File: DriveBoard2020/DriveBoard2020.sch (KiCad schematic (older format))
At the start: 56 parts, among them SW0 SW_SPST, SW1 SW_Push, SW2 SW_Push, SW3 SW_Push, SW4 SW_Push, SW5 SW_Push, SW6 SW_Push, U1 MAX232, U2 MAX232, U3 OKI, U4 TM4C129E_Launchpad, U5 MAX232, U6 OKI

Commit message: switch level shifters to 3232's
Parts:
- removed U1, U2, U5: MAX232, Package_SO:SOIC-16_3.9x9.9mm_P1.27mm, symbol Interface_UART:MAX232
- added U? (x3): MAX_3232, symbol MRDT_ICs:MAX_3232
- Conn1: symbol DriveBoard2020-rescue:AndersonPP-MRDT_Connectors -> DriveBoard2020-rescue:AndersonPP-MRDT_Connectors-DriveBoard2020-rescue
- Conn2, Conn3, Conn4, Conn5, Conn6, Conn7: symbol DriveBoard2020-rescue:Molex_SL_05-MRDT_Connectors -> DriveBoard2020-rescue:Molex_SL_05-MRDT_Connectors-DriveBoard2020-rescue
- U3, U6: symbol DriveBoard2020-rescue:OKI-MRDT_Devices -> DriveBoard2020-rescue:OKI-MRDT_Devices-DriveBoard2020-rescue
- U4: symbol DriveBoard2020-rescue:TM4C129E_Launchpad-MRDT_Shields -> DriveBoard2020-rescue:TM4C129E_Launchpad-MRDT_Shields-DriveBoard2020-rescue
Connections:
- wire segments 117 -> 124
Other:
- moved on the sheet: C3, C4, D10, D11, D12, D13, D14, D8, D9, R10, R11, R12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

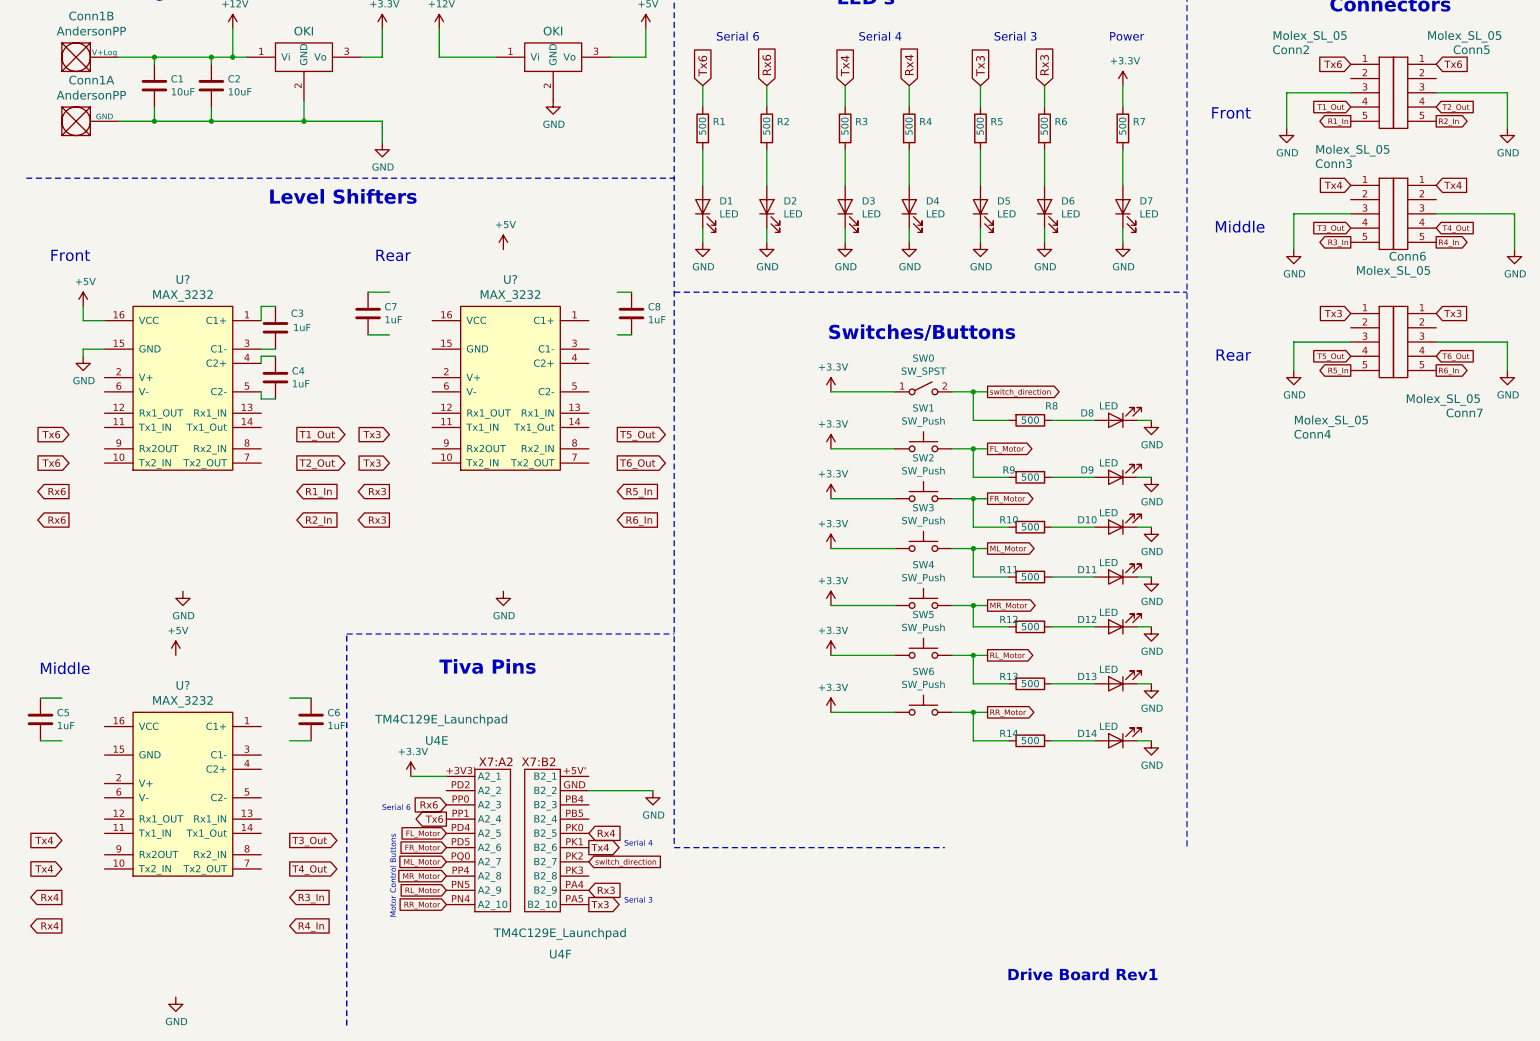
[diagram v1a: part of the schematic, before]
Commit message: changed and wired 3232's
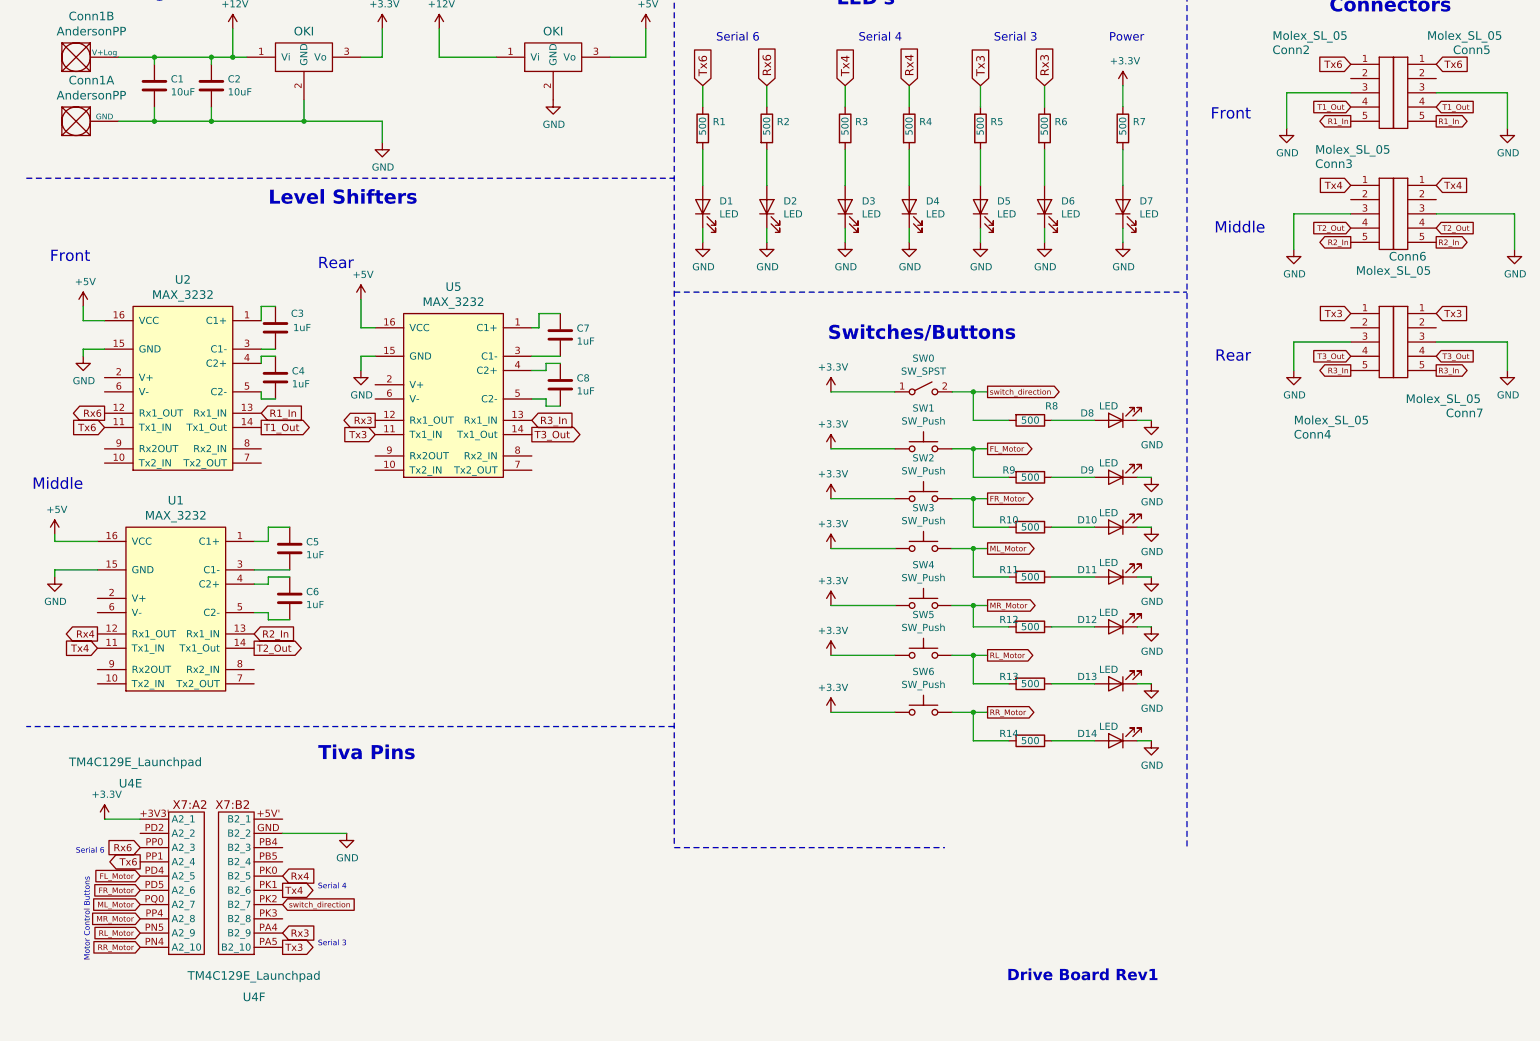
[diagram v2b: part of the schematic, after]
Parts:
- U1, U2, U5: renamed from U?; footprint (none) -> Package_SO:SOIC-16_3.9x9.9mm_P1.27mm
- U4: footprint MRDT_Shields:TM4C129E_Launchpad_X7_THT_BOTTOM -> MRDT_Shields:TM4C129E_Launchpad_FULL_THT_BOTTOM
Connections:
- net labels removed: R4_In, R5_In, R6_In, T4_Out, T5_Out, T6_Out
- wire segments 124 -> 144
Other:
- moved on the sheet: C5, C6, C7, C8, U1, U4E, U4F, U5

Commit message: Added lighting stuff
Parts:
- added C?: 10uF, Capacitor_SMD:C_0603_1608Metric_Pad1.05x0.95mm_HandSolder, symbol Device:C_Small
- added C? (x2): 10uF, Capacitor_SMD:C_0603_1608Metric_Pad1.05x0.95mm_HandSolder, symbol Device:C
- added Conn? (x2): Molex_SL_02, MRDT_Connectors:MOLEX_SL_02_Horizontal, symbol MRDT_Connectors:Molex_SL_02
- added Conn?: Molex_SL_03, MRDT_Connectors:MOLEX_SL_03_Horizontal, symbol MRDT_Connectors:Molex_SL_03
- added Conn?: AndersonPP, symbol MRDT_Connectors:AndersonPP
- added D? (x2): G_LED, LED_SMD:LED_0603_1608Metric_Pad1.05x0.95mm_HandSolder, symbol Device:LED
- added D? (x2): Org_LED, LED_SMD:LED_0603_1608Metric_Pad1.05x0.95mm_HandSolder, symbol Device:LED
- added R? (x4): 500, Resistor_SMD:R_0603_1608Metric_Pad1.05x0.95mm_HandSolder, symbol Device:R
- added R? (x3): 10K, Resistor_SMD:R_0603_1608Metric_Pad1.05x0.95mm_HandSolder, symbol Device:R
- added SW? (x3): SW_Push, Button_Switch_SMD:SW_SPST_TL3305A, symbol Switch:SW_Push
- added U? (x2): TM4C129E_Launchpad, MRDT_Shields:TM4C129E_Launchpad_X9_SMD, symbol MRDT_Shields:TM4C129E_Launchpad
- added U? (x2): LDD-1500L, MRDT_Devices:LDD-1500L_LED_DRIVER, symbol MRDT_Devices:LDD-1500L
- added U?: OKI, MRDT_Devices:OKI_Horizontal, symbol DriveBoard2020-rescue:OKI-MRDT_Devices-DriveBoard2020-rescue
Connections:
- net GND: now also C?.2, C?.2, C?.2, Conn?.3, D?.1 (K), D?.1 (K), D?.1 (K), D?.1 (K), R?.1, R?.1, R?.1, U?.1 (-Vin), U?.1 (-Vin), U?.2 (-Vin), U?.2 (-Vin), U?.2 (GND), U?.GND (D1_1)
- new net: D?.2 (A), R?.2 (x4)
- new net +12VA: C?.1, C?.1, Conn?.3 (V+Act), U?.1 (Vi), U?.23 (+Vin), U?.23 (+Vin), U?.24 (+Vin), U?.24 (+Vin)
- new net +5VA: C?.1, Conn?.1, R?.1, U?.3 (Vo)
- new net +5VL: R?.1, SW?.1, SW?.1, SW?.1
- new net Dout_NeoPixel: Conn?.2, R?.1, U?.PF1 (C1_1)
- new net Headlight_OnOff_PWM: R?.1, U?.21 (PWM_In), U?.21 (PWM_In), U?.PL3 (C1_10)
- new net Headlight_Power: R?.2, SW?.2, U?.PM3 (D1_2)
- new net Headlight_V1+: Conn?.1, U?.13 (+Vout), U?.14 (+Vout)
- new net Headlight_V1-: Conn?.2, U?.11 (-Vout), U?.12 (-Vout)
- new net Headlight_V2+: Conn?.1, U?.13 (+Vout), U?.14 (+Vout)
- new net Headlight_V2-: Conn?.2, U?.11 (-Vout), U?.12 (-Vout)
- new net NeoPixel_Pattern: R?.2, SW?.2, U?.PL5 (C1_6)
- new net NeoPixel_White: R?.2, SW?.2, U?.PL4 (C1_5)
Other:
- note added: "Indicators"
- note added: "Indicators (Drive)"
- note added: "LED_Drivers"
- note added: "NeoPixel_Strip"
- note added: "Push Buttons (Lighting)"
- note added: "SPI MOSI(3)"
- note added: "TIVA_C"
- note removed: "Drive Board Rev1"
- note removed: "LED's"
- moved on the sheet: C1, C2, C3, C4, C5, C6, C7, C8, Conn1A, Conn1B, Conn2, Conn3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

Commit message: assigned some footprints
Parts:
- Conn8: renamed from Conn?; footprint (none) -> MRDT_Connectors:Anderson_2_Horizontal_Side_by_Side
- gave numbers to parts that had none: 24

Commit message: worked on integrating lighting and drive board schematic
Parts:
- removed C11: 10uF, Capacitor_SMD:C_0603_1608Metric_Pad1.05x0.95mm_HandSolder, symbol Device:C_Small
- removed Conn9: Molex_SL_03, MRDT_Connectors:MOLEX_SL_03_Horizontal, symbol MRDT_Connectors:Molex_SL_03
- removed U9: LDD-1500L, MRDT_Devices:LDD-1500L_LED_DRIVER, symbol MRDT_Devices:LDD-1500L
- added Conn9: Molex_SL_02, MRDT_Connectors:MOLEX_SL_02_Horizontal, symbol MRDT_Connectors:Molex_SL_02
- added U9: TM4C129E_Launchpad, symbol MRDT_Shields:TM4C129E_Launchpad
- U10: footprint MRDT_Shields:TM4C129E_Launchpad_X9_SMD -> (none)
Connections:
- net Headlight_V2+ is gone; now on net Dout_NeoPixel: Conn11.1
- net Headlight_V2- is gone; now on net GND: Conn11.2
- net Dout_NeoPixel: now also Conn9.1
- net GND: now also Conn9.2, U9.GND (B1_2), U9.GND (D2_1); no longer D15.1 (K)
- net Headlight_OnOff_PWM: now also U9.PA7 (D2_4); no longer U10.PL3 (C1_10)
- new net GNDA: D15.1 (K)
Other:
- note added: "Lighting"
- note removed: "Limit voltage"
- note removed: "TIVA_C"
- moved on the sheet: C1, C10, C2, C3, C4, C5, C6, C7, C8, C9, Conn10, Conn1A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

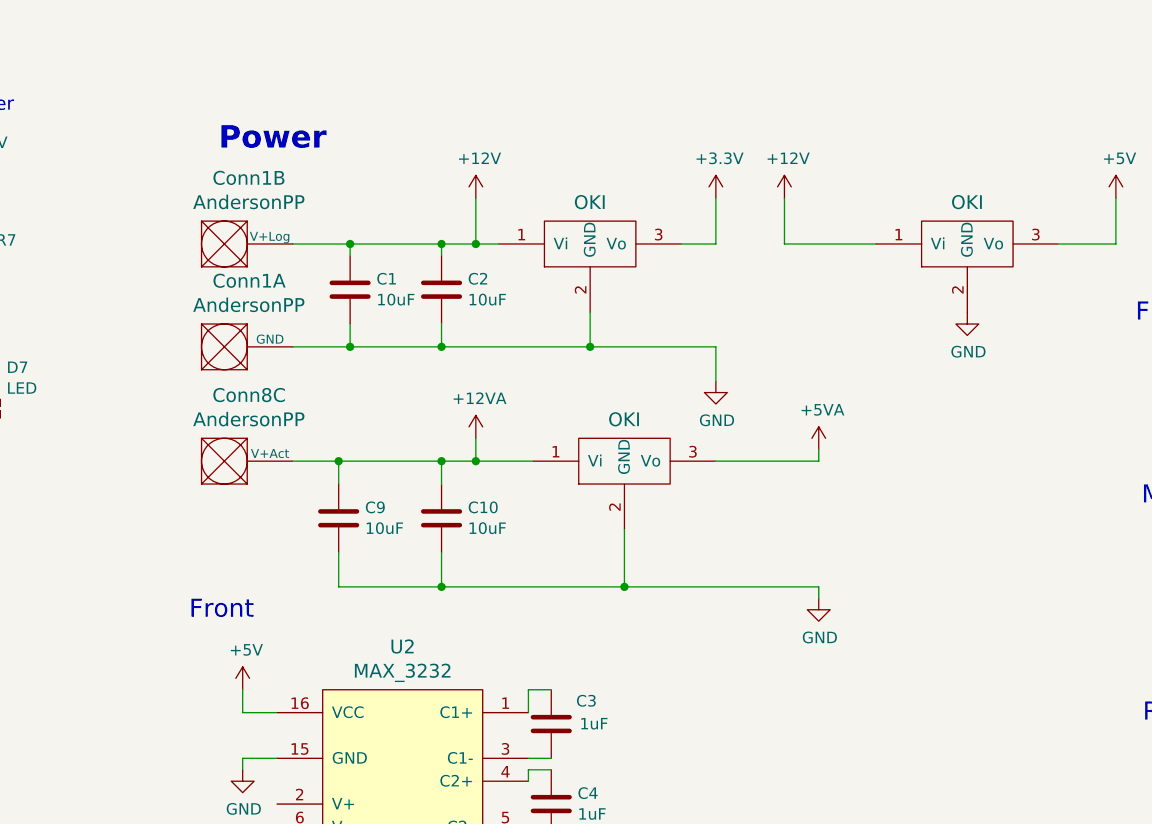
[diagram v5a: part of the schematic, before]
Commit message: created netlist, began layout
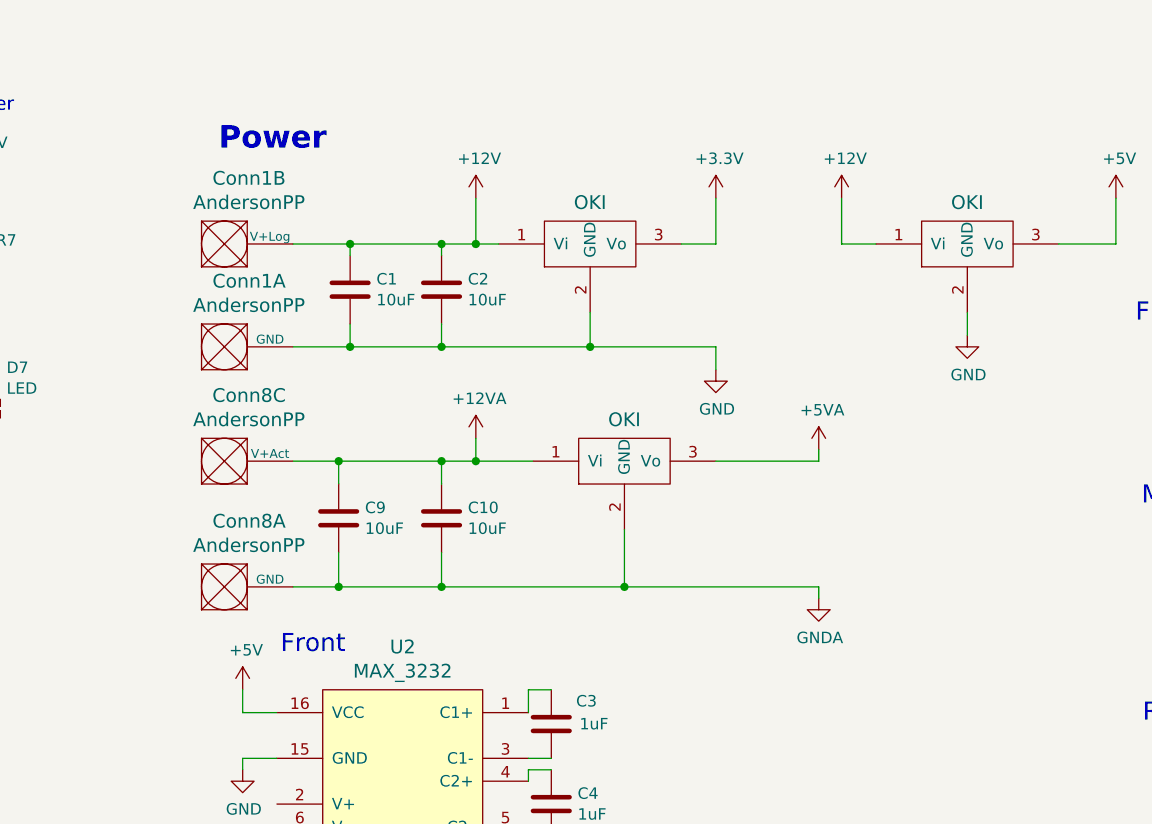
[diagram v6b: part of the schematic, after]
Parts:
- added unit 1 of Conn8
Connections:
- net GND: no longer C10.2, C9.2, U7.2 (GND)
- net GNDA: now also C10.2, C9.2, U7.2 (GND), Conn8.1 (GND)
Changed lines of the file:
@@
 	4600 1150 4600 950
-Wire Wire Line
-	3150 1150 3150 950
 Wire Wire Line
 	1800 1150 1900 1150
@@
 Wire Wire Line
 	1650 1150 1800 1150
-$Comp
-L power:GND #PWR0139
-U 1 1 5DA0B766
-P 3950 1450
-F 0 "#PWR0139" H 3950 1200 50  0001 C CNN
-F 1 "GND" H 3955 1277 50  0000 C CNN
-F 2 "" H 3950 1450 50  0001 C CNN
-F 3 "" H 3950 1450 50  0001 C CNN
-	1    3950 1450
-	1    0    0    -1
-$EndComp
 $Comp
 L power:+5V #PWR0109
@@
 F 3 "" H 3550 1150 60  0001 C CNN
 	1    3750 1250
-	1    0    0    -1
-$EndComp
-Wire Wire Line
-	3150 1150 3550 1150
-$Comp
-L power:+12V #PWR0107
-U 1 1 5D9FF58C
-P 3150 950
-F 0 "#PWR0107" H 3150 800 50  0001 C CNN
-F 1 "+12V" H 3165 1123 50  0000 C CNN
-F 2 "" H 3150 950 50  0001 C CNN
-F 3 "" H 3150 950 50  0001 C CNN
-	1    3150 950
 	1    0    0    -1
 $EndComp
@@
 Text Notes 900  4430 2    79   ~ 0
 Middle
-Text Notes 830  2800 2    79   ~ 0
+Text Notes 1230 2950 2    79   ~ 0
 Front
 $Comp
@@
 $EndComp
 Wire Wire Line
-	2300 1600 2850 1600
-Wire Wire Line
 	2850 1150 2850 950
 Wire Wire Line
 	2700 1150 2850 1150
-Connection ~ 2300 1600
-Wire Wire Line
-	2300 1450 2300 1600
-Wire Wire Line
-	1650 1600 2300 1600
-Connection ~ 1650 1600
 Wire Wire Line
 	1650 1500 1650 1600
@@
 	1    0    0    -1
 $EndComp
-$Comp
-L power:GND #PWR0101
-U 1 1 5D91E554
-P 2850 1750
-F 0 "#PWR0101" H 2850 1500 50  0001 C CNN
-F 1 "GND" H 2855 1577 50  0000 C CNN
-F 2 "" H 2850 1750 50  0001 C CNN
-F 3 "" H 2850 1750 50  0001 C CNN
-	1    2850 1750
-	1    0    0    -1
-$EndComp
-Wire Wire Line
-	2850 1600 2850 1750
 Wire Wire Line
 	1000 1150 1250 1150
@@
 Wire Wire Line
 	2450 2400 2450 2650
-$Comp
-L power:GND #PWR0166
-U 1 1 5E3E3046
-P 3300 2700
-F 0 "#PWR0166" H 3300 2450 50  0001 C CNN
-F 1 "GND" H 3305 2527 50  0000 C CNN
-F 2 "" H 3300 2700 50  0001 C CNN
-F 3 "" H 3300 2700 50  0001 C CNN
-	1    3300 2700
-	1    0    0    -1
-$EndComp
 Wire Wire Line
 	2450 2650 3300 2650
@@
 	4500 4470 4500 4490
 $Comp
-L power:GND #PWR?
+L power:GND #PWR0146
 U 1 1 5E44A8A8
 P 4500 4490
-F 0 "#PWR?" H 4500 4240 50  0001 C CNN
+F 0 "#PWR0146" H 4500 4240 50  0001 C CNN
 F 1 "GND" H 4505 4317 50  0000 C CNN
 F 2 "" H 4500 4490 50  0001 C CNN
@@
 	4080 4470 4500 4470
 $Comp
-L power:GND #PWR?
+L power:GND #PWR0150
 U 1 1 5E4D6DF7
 P 6740 6520
-F 0 "#PWR?" H 6740 6270 50  0001 C CNN
+F 0 "#PWR0150" H 6740 6270 50  0001 C CNN
 F 1 "GND" H 6745 6347 50  0000 C CNN
 F 2 "" H 6740 6520 50  0001 C CNN
@@
 Wire Wire Line
 	6430 6520 6740 6520
+$Comp
+L power:GNDA #PWR0151
+U 1 1 5E572CB7
+P 3300 2700
+F 0 "#PWR0151" H 3300 2450 50  0001 C CNN
+F 1 "GNDA" H 3305 2527 50  0000 C CNN
+F 2 "" H 3300 2700 50  0001 C CNN
+F 3 "" H 3300 2700 50  0001 C CNN
+	1    3300 2700
+	1    0    0    -1
+$EndComp
+$Comp
+L MRDT_Connectors:AndersonPP Conn8
+U 1 1 5E595C87
+P 600 2750
+F 0 "Conn8" H 808 3137 60  0000 C CNN
+F 1 "AndersonPP" H 808 3031 60  0000 C CNN
+F 2 "MRDT_Connectors:Anderson_2_Horizontal_Side_by_Side" H 450 2200 60  0001 C CNN
+F 3 "" H 450 2200 60  0001 C CNN
+	1    600  2750
+	1    0    0    -1
+$EndComp
+Wire Wire Line
+	1200 2650 1000 2650
+Connection ~ 1200 2650
+Wire Wire Line
+	1650 1600 2300 1600
+Connection ~ 1650 1600
+Wire Wire Line
+	2300 1450 2300 1600
+$Comp
+L power:+12V #PWR0101
+U 1 1 5E6D2E86
+P 3400 950
+F 0 "#PWR0101" H 3400 800 50  0001 C CNN
+F 1 "+12V" H 3415 1123 50  0000 C CNN
+F 2 "" H 3400 950 50  0001 C CNN
+F 3 "" H 3400 950 50  0001 C CNN
+	1    3400 950
+	1    0    0    -1
+$EndComp
+Wire Wire Line
+	3400 950  3400 1150
+Wire Wire Line
+	3400 1150 3550 1150
+Wire Wire Line
+	2300 1600 2850 1600
+Wire Wire Line
+	2850 1600 2850 1700
+Connection ~ 2300 1600
+$Comp
+L power:GND #PWR0107
+U 1 1 5E6F44C0
+P 2850 1700
+F 0 "#PWR0107" H 2850 1450 50  0001 C CNN
+F 1 "GND" H 2855 1527 50  0000 C CNN
+F 2 "" H 2850 1700 50  0001 C CNN
+F 3 "" H 2850 1700 50  0001 C CNN
+	1    2850 1700
+	1    0    0    -1
+$EndComp
+Wire Wire Line
+	3950 1450 3950 1550
+$Comp
+L power:GND #PWR0139
+U 1 1 5E77D4FB
+P 3950 1550
+F 0 "#PWR0139" H 3950 1300 50  0001 C CNN
+F 1 "GND" H 3955 1377 50  0000 C CNN
+F 2 "" H 3950 1550 50  0001 C CNN
+F 3 "" H 3950 1550 50  0001 C CNN
+	1    3950 1550
+	1    0    0    -1
+$EndComp
 $EndSCHEMATC
